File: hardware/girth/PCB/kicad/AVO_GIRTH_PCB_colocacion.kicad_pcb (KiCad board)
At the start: 4 copper layers, 65.5 x 43.5 mm, 122 parts, among them J1 USB-C 16P, J2 BATERÍA 1S, K1 G6KU-2F-Y DC3, Q1 AO3401A, Q10 AO3401A, Q11 AO3400A, Q12 2N7002, Q13 AO3400A, Q14 AO3401A, Q15 2N7002, Q16 2N7002, Q17 AO3401A, Q18 2N7002, Q2 AO3401A, Q3 AO3401A, SW1 REED (1), SW2 REED (2), U1 BQ51013BRHLR, U2 BQ24072RGTR, U3 RT9080-33GJ5, U4 ESP32-C6-MINI-1U-N4, U5 BNO085, U6 USBLC6-2SC6, Y1 32,768 kHz 12,5 pF

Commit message: PCB cincha: In2 como capa de ruteado (+3V3 rellena después), pines abiertos con su nombre de red, esquema sin solapes, condensadores Qi separados de los pines, reparación con rip-up
Co-Authored-By: Claude Opus 5.5 <noreply@anthropic.com>
Claude-Session: https://claude.ai/code/session_01CHDvF8BfHwPLkrFs9S3ECm
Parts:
- moved C6 2.42 mm to (78.1, 109.4)
- moved C8 2.42 mm to (80.7, 109.4)
- moved C7 2.33 mm to (79.4, 109.6)
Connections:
- D11 pad 2: (no net) -> unconnected-(D11-A2-Pad2)
- J1 pad A8: (no net) -> unconnected-(J1-SBU1-PadA8)
- J1 pad B8: (no net) -> unconnected-(J1-SBU2-PadB8)
- U2 pad 14: (no net) -> unconnected-(U2-TMR-Pad14)
- U3 pad 4: (no net) -> unconnected-(U3-NC-Pad4)
- U4 pad 21: (no net) -> unconnected-(U4-NC-Pad21)
- U4 pad 32: (no net) -> unconnected-(U4-NC-Pad32)
- U4 pad 33: (no net) -> unconnected-(U4-NC-Pad33)
- U4 pad 34: (no net) -> unconnected-(U4-NC-Pad34)
- U4 pad 35: (no net) -> unconnected-(U4-NC-Pad35)
- U4 pad 4: (no net) -> unconnected-(U4-NC-Pad4)
- U4 pad 7: (no net) -> unconnected-(U4-NC-Pad7)
- U5 pad 1: (no net) -> unconnected-(U5-NC-Pad1)
- U5 pad 12: (no net) -> unconnected-(U5-NC-Pad12)
- U5 pad 13: (no net) -> unconnected-(U5-NC-Pad13)
- U5 pad 21: (no net) -> unconnected-(U5-NC-Pad21)
- U5 pad 22: (no net) -> unconnected-(U5-NC-Pad22)
- U5 pad 23: (no net) -> unconnected-(U5-NC-Pad23)
- U5 pad 24: (no net) -> unconnected-(U5-NC-Pad24)
- U5 pad 7: (no net) -> unconnected-(U5-NC-Pad7)
- U5 pad 8: (no net) -> unconnected-(U5-NC-Pad8)
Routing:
- net VIN5: track 35.0 -> 0.00 mm, vias 2 -> 0
- net CHG_STAT: track 33.8 -> 4.29 mm, vias 3 -> 0
- net QI_CHG: track 0.00 -> 7.91 mm
- net QI_RECT: track 17.3 -> 12.8 mm, vias 0 -> 2
- net CC2: track 9.70 -> 6.21 mm, vias 0 -> 2
- net CHG_PG: track 0.00 -> 3.00 mm, vias 0 -> 2
- net VBAT: track 60.4 -> 57.7 mm, vias 4 -> 0
- net QI_BOOT1: track 2.17 -> 4.71 mm
- net QI_CLAMP1: track 2.26 -> 4.47 mm
- net QI_COMM1: track 2.61 -> 4.27 mm
- net VBUS: track 69.1 -> 69.6 mm, vias 10 -> 8
- net +3V3: track 0.45 -> 0.00 mm, vias 15 -> 0
- net CHG_EN2: track 2.96 -> 3.37 mm, vias 2 -> 0
- net VSYS: track 49.7 -> 49.6 mm, vias 0 -> 2
- net CHG_ISET: track 1.47 -> 1.45 mm, vias 2 -> 0
- removed copper zone on In2.Cu, net +3V3

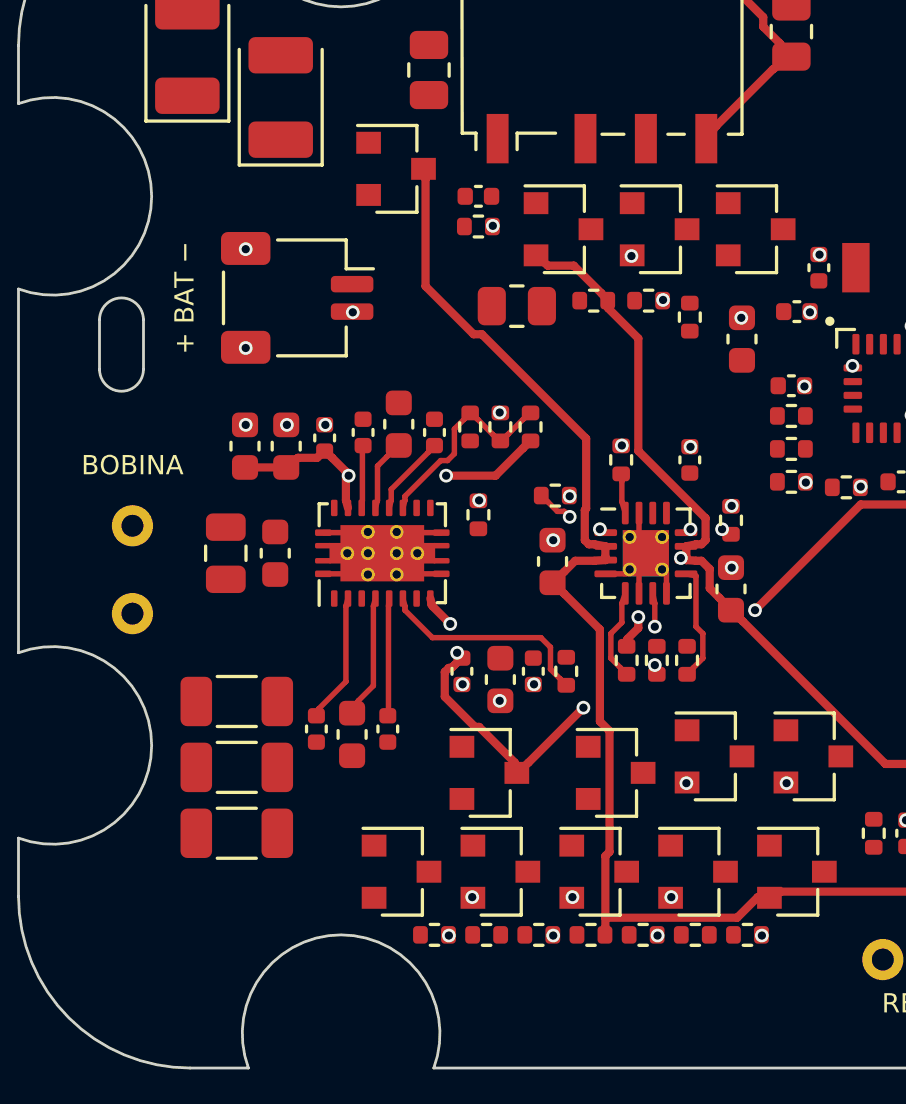
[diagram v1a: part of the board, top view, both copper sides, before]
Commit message: PCB cincha: entorno del BQ51013B reordenado (salida limpia de pines), símbolos por disposición de pines
Co-Authored-By: Claude Opus 5.5 <noreply@anthropic.com>
Claude-Session: https://claude.ai/code/session_01CHDvF8BfHwPLkrFs9S3ECm
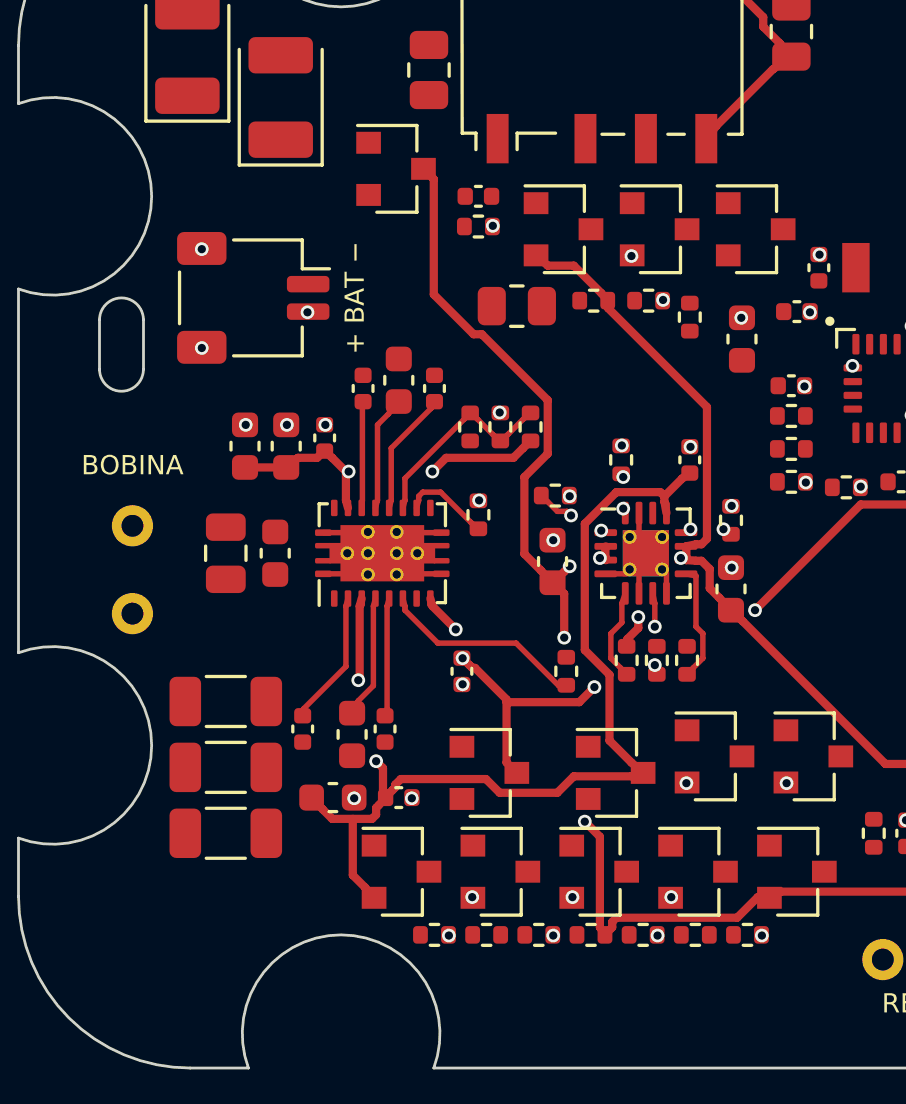
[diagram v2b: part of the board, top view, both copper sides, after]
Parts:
- moved C15 7.46 mm to (78.7, 111.9), turned to 0 degrees
- moved C16 6.72 mm to (81.1, 111.9), turned to 0 degrees
- moved J2 1.60 mm to (75.8, 93.7)
- moved C10 1.60 mm to (81.1, 96.7)
- moved C11 1.60 mm to (82.4, 97.0)
- moved C9 1.60 mm to (79.8, 97.0)
- moved C6 0.50 mm to (77.6, 109.4)
- moved C1 0.40 mm to (74.8, 108.4)
- moved C2 0.40 mm to (74.8, 110.8)
- moved C3 0.40 mm to (74.8, 113.2)
- moved C8 0.10 mm to (80.6, 109.4)
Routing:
- net VIN5: track 0.00 -> 39.8 mm, vias 0 -> 2
- net QI_TS: track 0.00 -> 3.21 mm
- net QI_BOOT2: track 2.27 -> 3.87 mm
- net QI_COMM2: track 2.93 -> 4.51 mm
- net QI_CLAMP2: track 2.61 -> 4.19 mm
- net VBUS: track 69.6 -> 68.4 mm
- net VBAT: track 57.7 -> 58.9 mm, vias 0 -> 4
- net CHG_ISET: track 1.45 -> 1.47 mm, vias 0 -> 2
